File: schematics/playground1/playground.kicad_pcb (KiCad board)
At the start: 2 copper layers, 92.5 x 68.5 mm, 65 parts, among them J1 Conn_01x05, J2 Conn_02x03_Odd_Even, J3 Conn_01x03, J4 Conn_02x04_Odd_Even, SW1 SW_SPST, SW2 SW_Push, SW3 SW_Push, U1 ADS1299, U2 MCP1700x-330xxTT, U3 PIC32MX250F128B_I_SS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

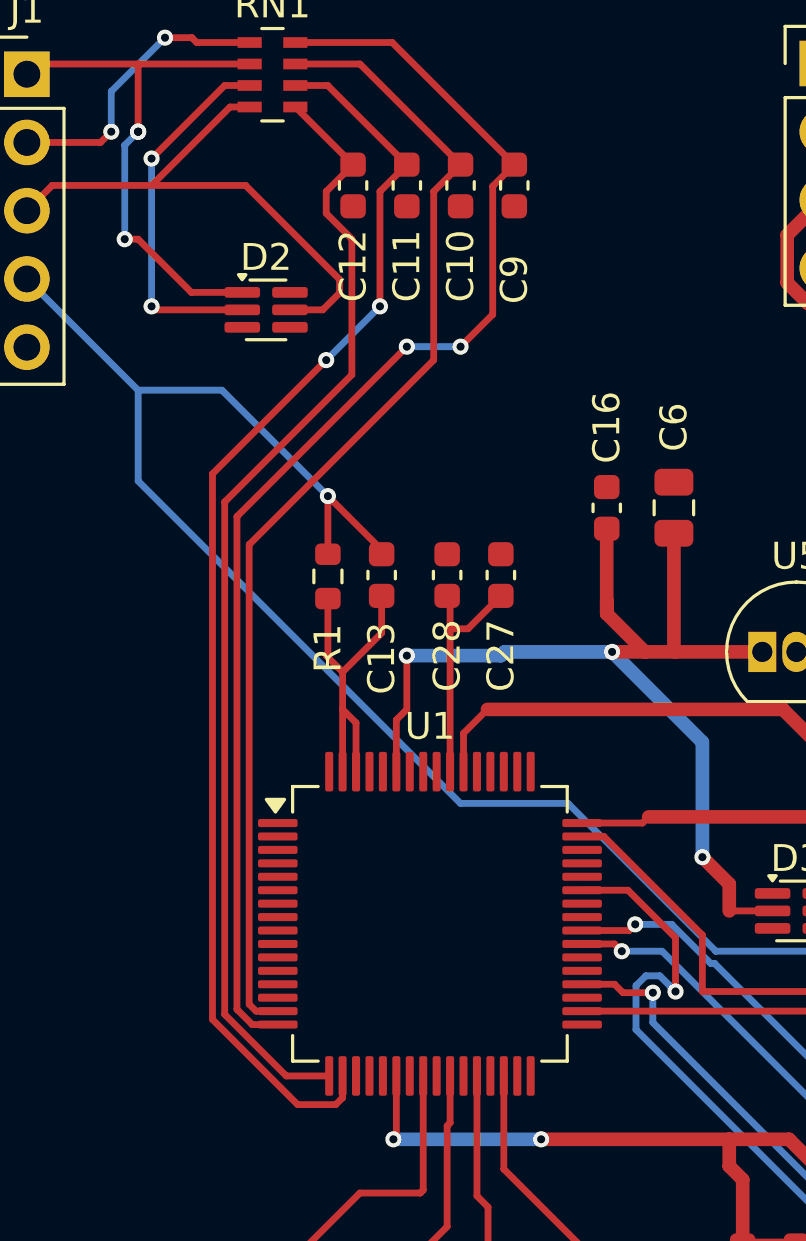
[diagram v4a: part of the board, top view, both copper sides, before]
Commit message: fixing unconnected items drc errors
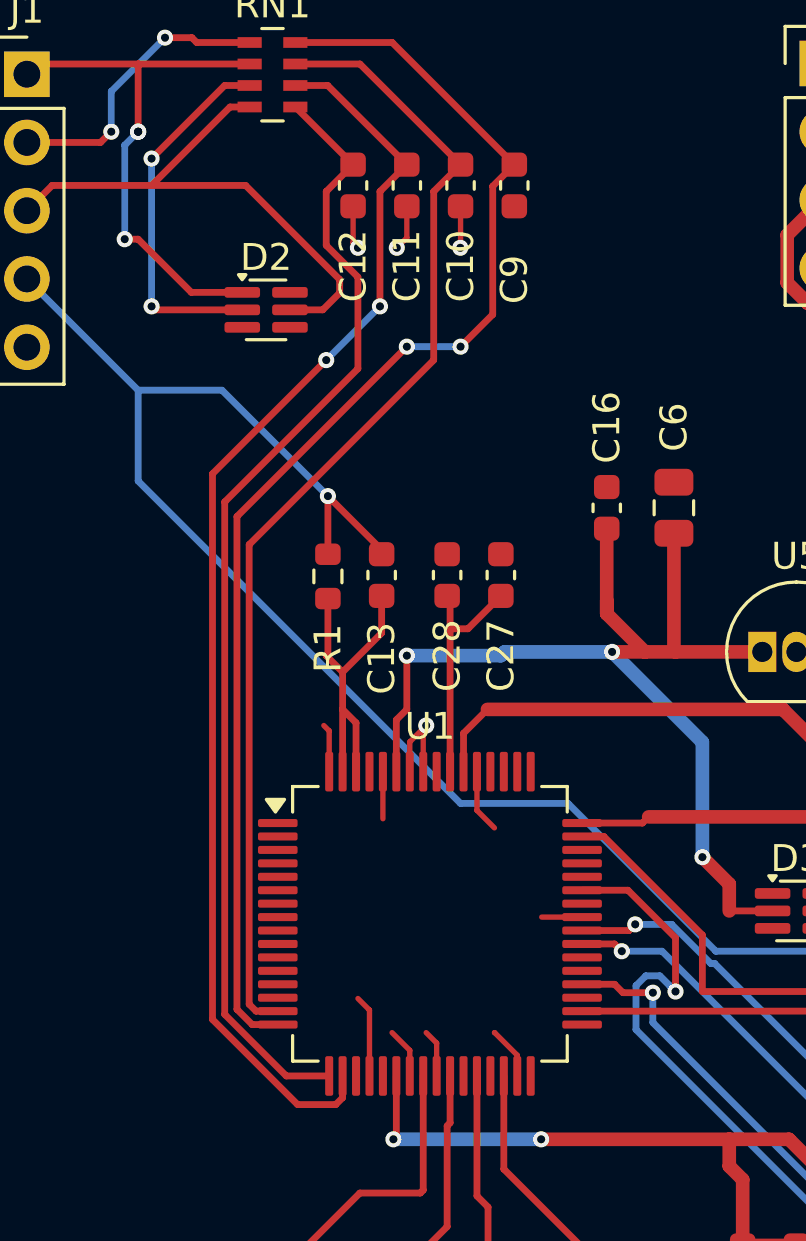
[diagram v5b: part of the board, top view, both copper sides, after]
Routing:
- net /AGND: track 0.00 -> 24.7 mm, vias 0 -> 4
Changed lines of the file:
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@@
+	)
+	(segment
+		(start 115.0225 108.73)
+		(end 113.52 108.73)
+		(width 0.2)
+		(layer "F.Cu")
+		(net 2)
+	)
+	(segment
+		(start 110.5 82.275)
+		(end 110.5 83.81)
+		(width 0.2)
+		(layer "F.Cu")
+		(net 2)
+	)
+	(segment
+		(start 108.5 83.447)
+		(end 108.127 83.82)
+		(width 0.2)
+		(layer "F.Cu")
+		(net 2)
+	)
+	(segment
+		(start 111.11 103.3175)
+		(end 111.11 104.76)
+		(width 0.2)
+		(layer "F.Cu")
+		(net 2)
+	)
+	(segment
+		(start 110.5 83.81)
+		(end 110.49 83.82)
+		(width 0.2)
+		(layer "F.Cu")
+		(net 2)
+	)
+	(segment
+		(start 111.768824 113.03)
+		(end 111.76 113.03)
+		(width 0.2)
+		(layer "F.Cu")
+		(net 2)
+	)
+	(segment
+		(start 108.5 82.275)
+		(end 108.5 83.447)
+		(width 0.2)
+		(layer "F.Cu")
+		(net 2)
+	)
+	(segment
+		(start 108.61 113.69)
+		(end 107.95 113.03)
+		(width 0.2)
+		(layer "F.Cu")
+		(net 2)
+	)
+	(segment
+		(start 108.61 102.21)
+		(end 109.22 101.6)
+		(width 0.2)
+		(layer "F.Cu")
+		(net 2)
+	)
+	(segment
+		(start 111.11 104.76)
+		(end 111.76 105.41)
+		(width 0.2)
+		(layer "F.Cu")
+		(net 2)
+	)
+	(segment
+		(start 107.11 114.6425)
+		(end 107.11 112.19)
+		(width 0.2)
+		(layer "F.Cu")
+		(net 2)
+	)
+	(segment
+		(start 109.11 103.3175)
+		(end 109.11 101.71)
+		(width 0.2)
+		(layer "F.Cu")
+		(net 2)
+	)
+	(segment
+		(start 105.61 101.8)
+		(end 105.41 101.6)
+		(width 0.2)
+		(layer "F.Cu")
+		(net 2)
+	)
+	(segment
+		(start 109.61 114.6425)
+		(end 109.61 113.42)
+		(width 0.2)
+		(layer "F.Cu")
+		(net 2)
+	)
+	(segment
+		(start 109.11 101.71)
+		(end 109.22 101.6)
+		(width 0.2)
+		(layer "F.Cu")
+		(net 2)
+	)
+	(segment
+		(start 106.5 82.275)
+		(end 106.5 83.64)
+		(width 0.2)
+		(layer "F.Cu")
+		(net 2)
+	)
+	(segment
+		(start 107.61 103.3175)
+		(end 107.61 105.07)
+		(width 0.2)
+		(layer "F.Cu")
+		(net 2)
+	)
+	(segment
+		(start 109.61 113.42)
+		(end 109.22 113.03)
+		(width 0.2)
+		(layer "F.Cu")
+		(net 2)
+	)
+	(segment
+		(start 112.61 113.871176)
+		(end 111.768824 113.03)
+		(width 0.2)
+		(layer "F.Cu")
+		(net 2)
+	)
+	(segment
+		(start 107.11 112.19)
+		(end 106.68 111.76)
+		(width 0.2)
+		(layer "F.Cu")
+		(net 2)
+	)
+	(segment
+		(start 105.61 103.3175)
+		(end 105.61 101.8)
+		(width 0.2)
+		(layer "F.Cu")
+		(net 2)
+	)
+	(segment
+		(start 108.61 114.6425)
+		(end 108.61 113.69)
+		(width 0.2)
+		(layer "F.Cu")
+		(net 2)
+	)
+	(segment
+		(start 112.61 114.6425)
+		(end 112.61 113.871176)
+		(width 0.2)
+		(layer "F.Cu")
+		(net 2)
+	)
+	(segment
+		(start 106.5 83.64)
+		(end 106.68 83.82)
+		(width 0.2)
+		(layer "F.Cu")
+		(net 2)
+	)
+	(segment
+		(start 108.61 103.3175)
+		(end 108.61 102.21)
+		(width 0.2)
+		(layer "F.Cu")
+		(net 2)
+	)
+	(via
+		(at 108.127 83.82)
+		(size 0.6)
+		(drill 0.3)
+		(layers "F.Cu" "B.Cu")
+		(net 2)
+	)
+	(via
+		(at 110.49 83.82)
+		(size 0.6)
+		(drill 0.3)
+		(layers "F.Cu" "B.Cu")
+		(net 2)
+	)
+	(via
+		(at 106.68 83.82)
+		(size 0.6)
+		(drill 0.3)
+		(layers "F.Cu" "B.Cu")
+		(net 2)
+	)
+	(via
+		(at 109.22 101.6)
+		(size 0.6)
+		(drill 0.3)
+		(layers "F.Cu" "B.Cu")
+		(net 2)
 	)
 	(segment
@@
 	)
 	(segment
+		(start 105.5 83.73)
+		(end 106.68 84.91)
+		(width 0.254)
+		(layer "F.Cu")
+		(net 14)
+	)
+	(segment
 		(start 104.35 78.58)
 		(end 104.355 78.58)
@@
 	)
 	(segment
-		(start 105.5 82.538294)
+		(start 106.68 84.91)
+		(end 106.68 88.32)
+		(width 0.254)
+		(layer "F.Cu")
+		(net 14)
+	)
+	(segment
+		(start 101.722 93.278)
+		(end 101.722 112.350942)
+		(width 0.254)
+		(layer "F.Cu")
+		(net 14)
+	)
+	(segment
+		(start 101.722 112.350942)
+		(end 104.013558 114.6425)
+		(width 0.254)
+		(layer "F.Cu")
+		(net 14)
+	)
+	(segment
+		(start 104.013558 114.6425)
+		(end 105.61 114.6425)
+		(width 0.254)
+		(layer "F.Cu")
+		(net 14)
+	)
+	(segment
+		(start 106.5 80.725)
 		(end 105.5 81.725)
 		(width 0.254)
@@
 	)
 	(segment
-		(start 106.455 83.493294)
-		(end 105.5 82.538294)
-		(width 0.254)
-		(layer "F.Cu")
-		(net 14)
-	)
-	(segment
-		(start 106.455 88.545)
-		(end 106.455 83.493294)
-		(width 0.254)
-		(layer "F.Cu")
-		(net 14)
-	)
-	(segment
 		(start 105.5 81.725)
-		(end 106.5 80.725)
-		(width 0.254)
-		(layer "F.Cu")
-		(net 14)
-	)
-	(segment
-		(start 105.61 114.6425)
-		(end 104.013558 114.6425)
-		(width 0.254)
-		(layer "F.Cu")
-		(net 14)
-	)
-	(segment
-		(start 101.722 112.350942)
-		(end 101.722 93.278)
+		(end 105.5 83.73)
 		(width 0.254)
 		(layer "F.Cu")
@@
 	)
 	(segment
-		(start 101.722 93.278)
-		(end 106.455 88.545)
-		(width 0.254)
-		(layer "F.Cu")
-		(net 14)
-	)
-	(segment
-		(start 104.013558 114.6425)
-		(end 101.722 112.350942)
-		(width 0.254)
-		(layer "F.Cu")
+		(start 106.68 88.32)
+		(end 101.722 93.278)
+		(width 0.254)
+		(layer "F.Cu")

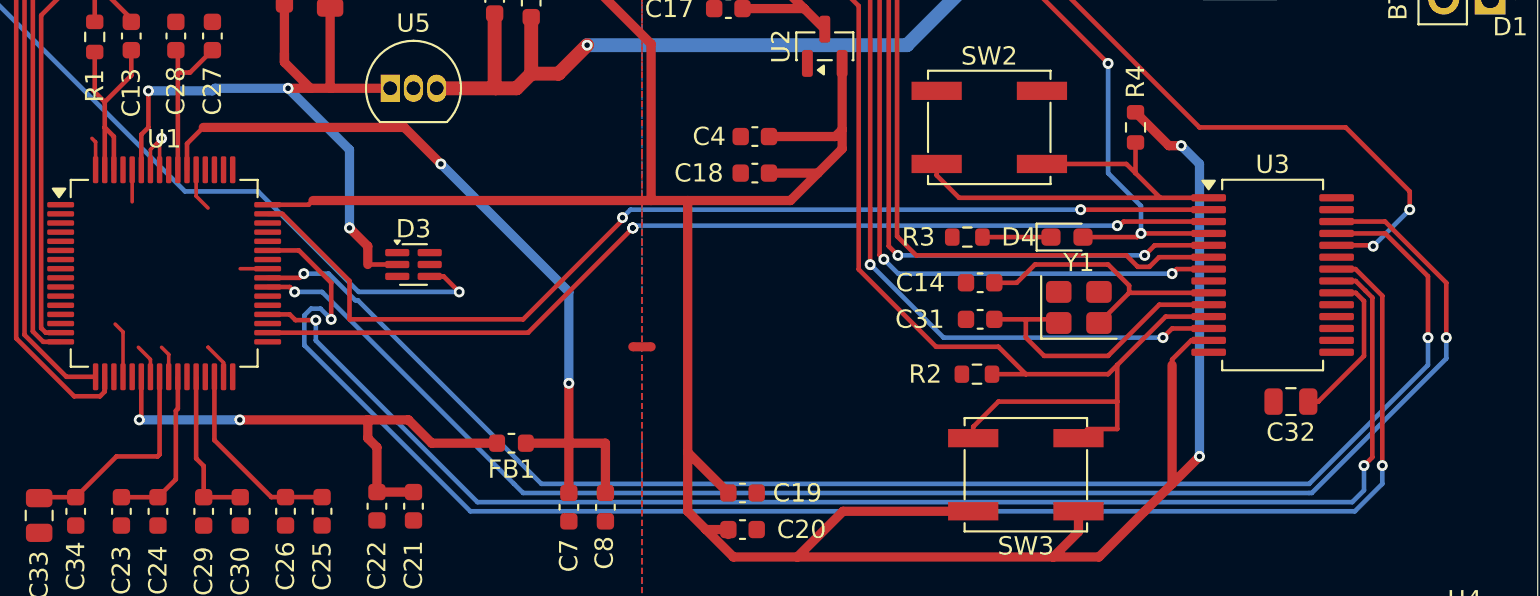
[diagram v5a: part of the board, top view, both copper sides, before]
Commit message: AGND connection issues fixed
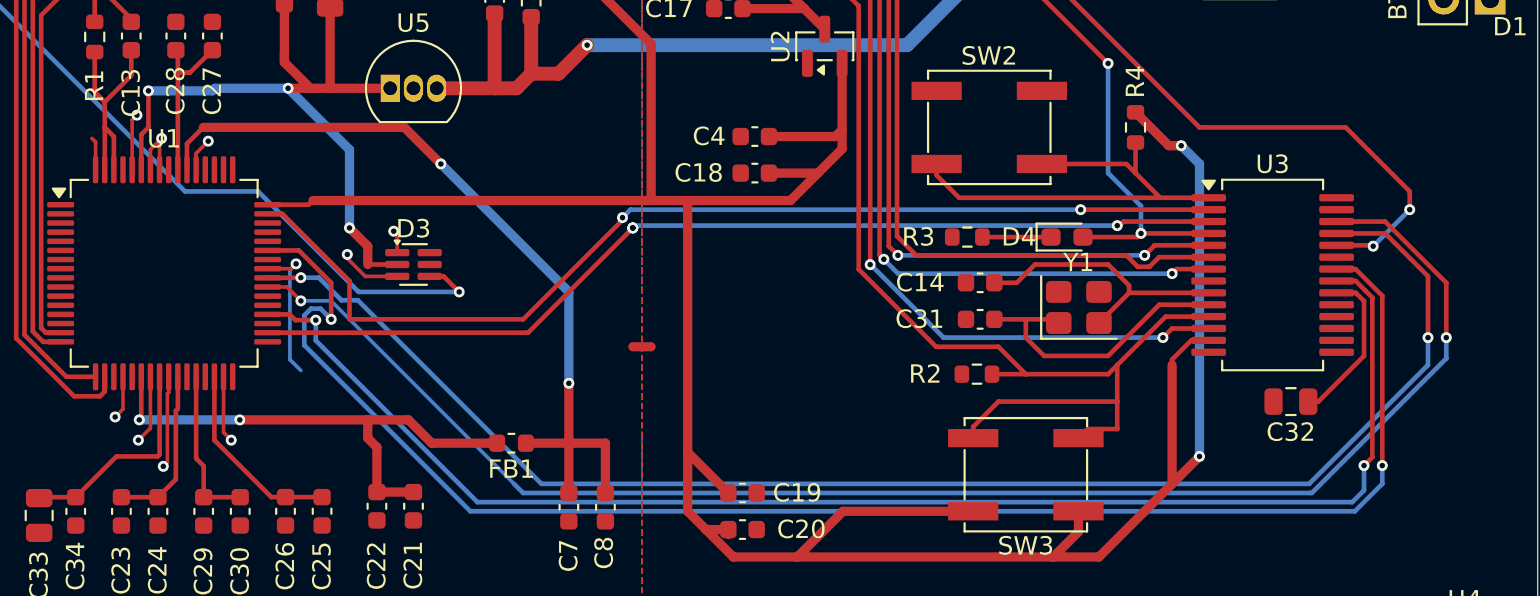
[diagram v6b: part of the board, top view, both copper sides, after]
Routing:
- net /AGND: track 24.7 -> 42.6 mm, vias 4 -> 13

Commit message: dgnd connection errors, some fixed
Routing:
- net /DGND: track 0.00 -> 28.5 mm, vias 0 -> 5
- net Net-(U3-VCAP): track 8.77 -> 11.9 mm
- net /MISO: track 86.8 -> 89.1 mm
- net /RESET: track 78.2 -> 79.8 mm
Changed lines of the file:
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@@
 			(pinfunction "Pin_4")
 			(pintype "passive")
+			(zone_connect 2)
 		)
 		(pad "5" thru_hole circle
@@
 	)
 	(segment
+		(start 175.26 111.510001)
+		(end 175.26 111.76)
+		(width 0.2)
+		(layer "F.Cu")
+		(net 7)
+	)
+	(segment
+		(start 146.05 108.065255)
+		(end 146.05 104.14)
+		(width 0.2)
+		(layer "F.Cu")
+		(net 7)
+	)
+	(segment
+		(start 164.622786 109.4)
+		(end 164.61192 109.389134)
+		(width 0.2)
+		(layer "F.Cu")
+		(net 7)
+	)
+	(segment
+		(start 153 114.5)
+		(end 152.484745 114.5)
+		(width 0.2)
+		(layer "F.Cu")
+		(net 7)
+	)
+	(segment
+		(start 175.17 105.5)
+		(end 175.26 105.41)
+		(width 0.2)
+		(layer "F.Cu")
+		(net 7)
+	)
+	(segment
+		(start 173.5 105.5)
+		(end 175.17 105.5)
+		(width 0.2)
+		(layer "F.Cu")
+		(net 7)
+	)
+	(segment
+		(start 166.5 109.4)
+		(end 164.622786 109.4)
+		(width 0.2)
+		(layer "F.Cu")
+		(net 7)
+	)
+	(segment
+		(start 154.215 110.49)
+		(end 156.21 110.49)
+		(width 0.2)
+		(layer "F.Cu")
+		(net 7)
+	)
+	(segment
+		(start 173.5 110.7)
+		(end 174.449999 110.7)
+		(width 0.2)
+		(layer "F.Cu")
+		(net 7)
+	)
+	(segment
+		(start 174.449999 110.7)
+		(end 175.26 111.510001)
+		(width 0.2)
+		(layer "F.Cu")
+		(net 7)
+	)
+	(segment
+		(start 152.484745 114.5)
+		(end 146.05 108.065255)
+		(width 0.2)
+		(layer "F.Cu")
+		(net 7)
+	)
+	(segment
+		(start 153.225 109.5)
+		(end 154.215 110.49)
+		(width 0.2)
+		(layer "F.Cu")
+		(net 7)
+	)
+	(via
+		(at 175.26 105.41)
+		(size 0.6)
+		(drill 0.3)
+		(layers "F.Cu" "B.Cu")
+		(net 7)
+	)
+	(via
+		(at 156.21 110.49)
+		(size 0.6)
+		(drill 0.3)
+		(layers "F.Cu" "B.Cu")
+		(net 7)
+	)
+	(via
+		(at 175.26 111.76)
+		(size 0.6)
+		(drill 0.3)
+		(layers "F.Cu" "B.Cu")
+		(net 7)
+	)
+	(via
+		(at 164.61192 109.389134)
+		(size 0.6)
+		(drill 0.3)
+		(layers "F.Cu" "B.Cu")
+		(net 7)
+	)
+	(via
+		(at 146.05 104.14)
+		(size 0.6)
+		(drill 0.3)
+		(layers "F.Cu" "B.Cu")
+		(net 7)
+	)
+	(segment
+		(start 164.61192 104.92192)
+		(end 163.83 104.14)
+		(width 0.2)
+		(layer "B.Cu")
+		(net 7)
+	)
+	(segment
+		(start 164.61192 109.389134)
+		(end 164.61192 104.92192)
+		(width 0.2)
+		(layer "B.Cu")
+		(net 7)
+	)
+	(segment
 		(start 120.5 107.5)
 		(end 119.5 106.5)
@@
 	)
 	(segment
-		(start 175 110.5)
-		(end 175 113.5)
-		(width 0.254)
+		(start 176.53 114.3)
+		(end 173.65 114.3)
+		(width 0.2)
 		(layer "F.Cu")
 		(net 22)
 	)
 	(segment
-		(start 174.55 110.05)
-		(end 175 110.5)
+		(start 172.5 116)
+		(end 171.95 116)
 		(width 0.254)
 		(layer "F.Cu")
@@
 	)
 	(segment
-		(start 172.5 116)
+		(start 173.65 114.3)
 		(end 171.95 116)
-		(width 0.254)
+		(width 0.2)
 		(layer "F.Cu")
 		(net 22)
@@
 	(segment
 		(start 173.5 110.05)
-		(end 174.55 110.05)
-		(width 0.254)
+		(end 174.449999 110.05)
+		(width 0.2)
 		(layer "F.Cu")
 		(net 22)
 	)
 	(segment
-		(start 175 113.5)
-		(end 172.5 116)
-		(width 0.254)
+		(start 174.449999 110.05)
+		(end 176.53 112.130001)
+		(width 0.2)
+		(layer "F.Cu")
+		(net 22)
+	)
+	(segment
+		(start 176.53 112.130001)
+		(end 176.53 114.3)
+		(width 0.2)
 		(layer "F.Cu")
 		(net 22)
@@
 	)
 	(segment
-		(start 164.5 109)
-		(end 164.75 108.75)
+		(start 148.5 107.985497)
+		(end 148.7294 108.214897)
 		(width 0.254)
 		(layer "F.Cu")
@@
 	)
 	(segment
-		(start 166.5 108.75)
-		(end 164.75 108.75)
+		(start 148.5 92.886712)
+		(end 148.5 107.985497)
 		(width 0.254)
 		(layer "F.Cu")
@@
 	)
 	(segment
-		(start 148.5 107.985497)
-		(end 148.7294 108.214897)
-		(width 0.254)
+		(start 164.3 108.75)
+		(end 163.83 109.22)
+		(width 0.2)
 		(layer "F.Cu")
 		(net 39)
 	)
 	(segment
-		(start 148.5 92.886712)
-		(end 148.5 107.985497)
+		(start 148.306644 92.693356)
+		(end 148.5 92.886712)
 		(width 0.254)
 		(layer "F.Cu")
@@
 	)
 	(segment
-		(start 148.306644 92.693356)
-		(end 148.5 92.886712)
-		(width 0.254)
+		(start 166.5 108.75)
+		(end 164.3 108.75)
+		(width 0.2)
 		(layer "F.Cu")
 		(net 39)
@@
 	)
 	(via
-		(at 164.5 109)
+		(at 163.83 109.22)
 		(size 0.6)
 		(drill 0.3)
@@
 	)
 	(segment
-		(start 147.5 79.5)
-		(end 150 77)
+		(start 148.7294 108.214897)
+		(end 149.514503 109)
 		(width 0.254)
 		(layer "B.Cu")
@@
 	)
 	(segment
-		(start 148.7294 108.214897)
-		(end 149.514503 109)
+		(start 147.5 79.5)
+		(end 150 77)
 		(width 0.254)
 		(layer "B.Cu")
@@
 	)
 	(segment
-		(start 149.514503 109)
-		(end 164.5 109)
-		(width 0.254)
+		(start 163.83 109.22)
+		(end 163.61 109)
+		(width 0.2)
 		(layer "B.Cu")
 		(net 39)
@@
 	)
 	(segment
+		(start 163.61 109)
+		(end 149.514503 109)
+		(width 0.2)
+		(layer "B.Cu")
+		(net 39)
+	)
+	(segment
 		(start 161.5 116)
 		(end 155 116)
@@
 	)
 	(segment
-		(start 116.543355 111.543355)
-		(end 116.23 111.23)
+		(start 177.345 117.155)
+		(end 175 119.5)
 		(width 0.254)
 		(layer "F.Cu")
@@
 	)
 	(segment
-		(start 175 119.5)
-		(end 175.455 119.045)
+		(start 116.543355 111.543355)
+		(end 116.23 111.23)
 		(width 0.254)
 		(layer "F.Cu")
@@
 	)
 	(segment
-		(start 175.455 119.045)
-		(end 175.455 110.311533)
+		(start 177.345 112.201534)
+		(end 177.345 117.155)
 		(width 0.254)
 		(layer "F.Cu")
@@
 	)
 	(segment
-		(start 117.656642 111.543355)
-		(end 116.543355 111.543355)
+		(start 174.543467 109.4)
+		(end 177.345 112.201534)
 		(width 0.254)
 		(layer "F.Cu")
@@
 	)
 	(segment
-		(start 175.455 110.311533)
-		(end 175.071733 109.928267)
+		(start 117.656642 111.543355)
+		(end 116.543355 111.543355)
 		(width 0.254)
 		(layer "F.Cu")
@@
 	)
 	(segment
-		(start 175.071733 109.928267)
+		(start 173.5 109.4)
 		(end 174.543467 109.4)
 		(width 0.254)
@@
 		(net 49)
 	)
-	(segment
-		(start 174.543467 109.4)
-		(end 173.5 109.4)
-		(width 0.254)
-		(layer "F.Cu")
-		(net 49)
-	)
 	(via
 		(at 117.656642 111.543355)
@@
 	)
 	(segment
-		(start 116.73 107.73)
-		(end 118.5 109.5)
+		(start 174.536934 108.75)
+		(end 173.5 108.75)
 		(width 0.254)
 		(layer "F.Cu")
@@
 	)
 	(segment
-		(start 115.0225 107.73)
-		(end 116.73 107.73)
+		(start 177.8 117.7)
+		(end 177.8 110.49)
 		(width 0.254)
 		(layer "F.Cu")
@@
 	)
 	(segment
-		(start 118.5 109.5)
-		(end 118.5 111.5)
+		(start 177.8 110.49)
+		(end 176.276934 110.49)
 		(width 0.254)
 		(layer "F.Cu")
@@
 	)
 	(segment
-		(start 174.536934 108.75)
-		(end 173.5 108.75)
+		(start 116.73 107.73)
+		(end 118.5 109.5)
+		(width 0.254)
+		(layer "F.Cu")
+		(net 71)
+	)
+	(segment
+		(start 176 119.5)
+		(end 177.8 117.7)
 		(width 0.254)
 		(layer "F.Cu")
@@
 	)
 	(segment
-		(start 176 110.213066)
+		(start 115.0225 107.73)
+		(end 116.73 107.73)
+		(width 0.254)
+		(layer "F.Cu")
+		(net 71)
+	)
+	(segment
+		(start 176.276934 110.49)
 		(end 174.536934 108.75)
 		(width 0.254)
@@
 	)
 	(segment
-		(start 176 119.5)
-		(end 176 110.213066)
+		(start 118.5 109.5)
+		(end 118.5 111.5)
 		(width 0.254)
 		(layer "F.Cu")

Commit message: avdd fixes
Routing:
- net /AVDD_5V: track 78.5 -> 90.4 mm
- net /AGND: track 42.6 -> 45.0 mm
